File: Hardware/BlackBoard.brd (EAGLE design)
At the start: 68.6 x 53.3 mm, 72 parts, among them IC3 LM1117, J1 microB, J2 ICSP, J3 POWER_JACKSUPER_BOMB_DIGITY, Q1 1A/60V/500mΩ, Q2 2N7002PW, Q3 2N7002PW, U2 CH340G, U3 AP2112-3.3V, U4 ATMEGA328P_TQFP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

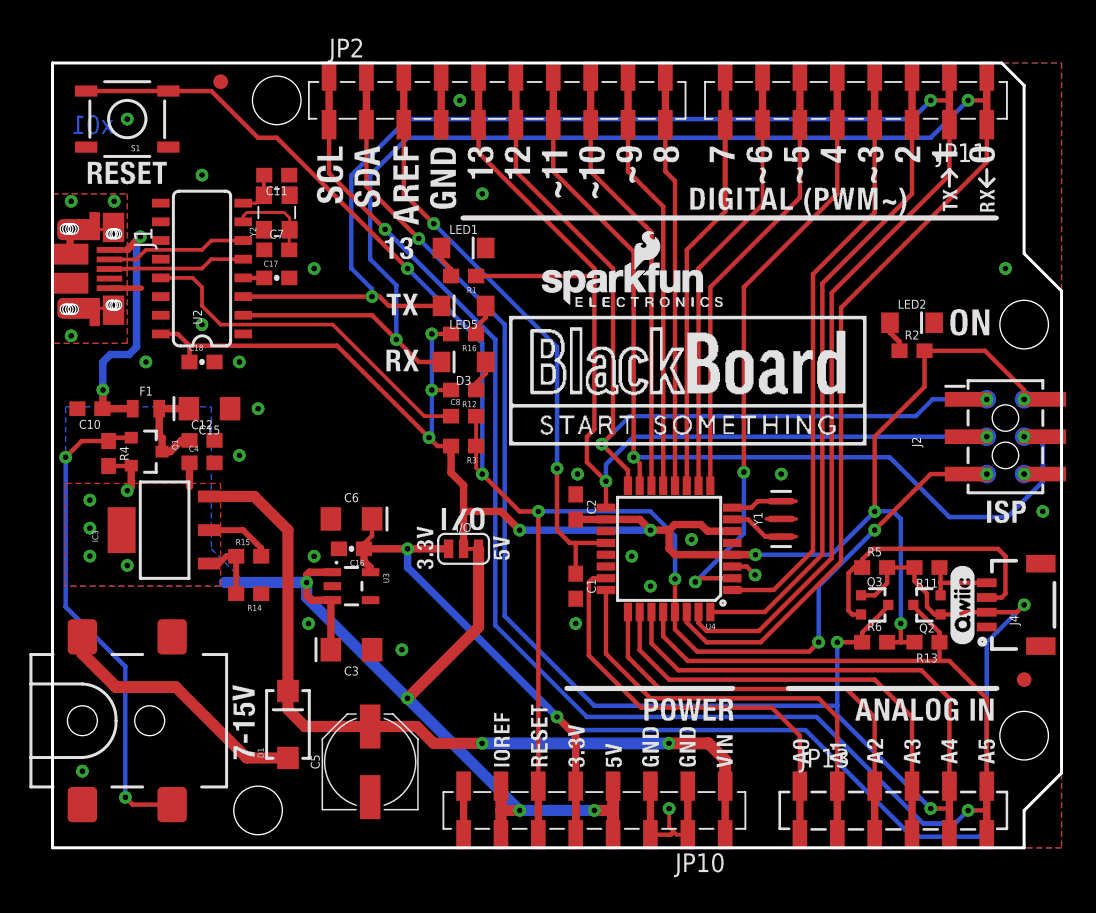
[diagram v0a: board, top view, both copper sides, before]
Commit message: Readme update. Schematic compression.
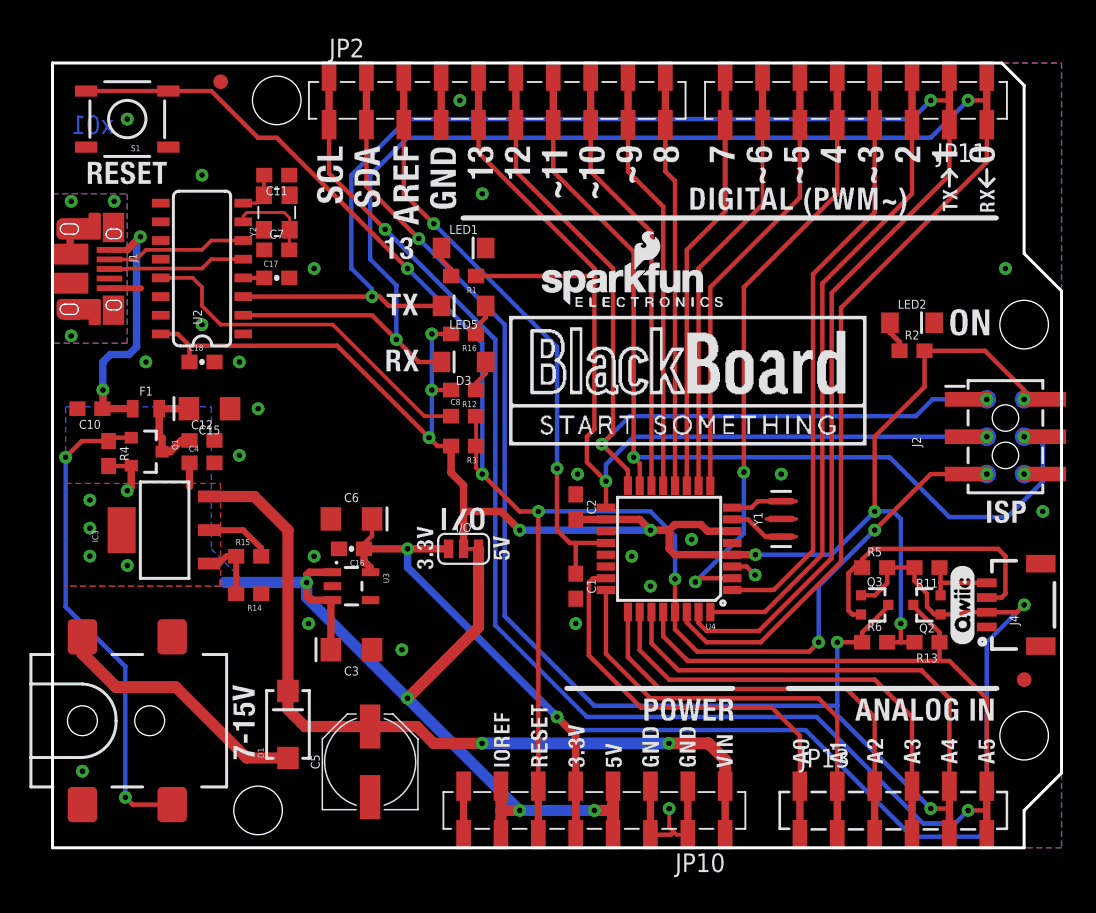
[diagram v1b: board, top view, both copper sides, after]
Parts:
- removed FRAME1: FRAME-LEDGER, SparkFun-Aesthetics:CREATIVE_COMMONS
- added FRAME2: FRAME-LETTER, SparkFun-Aesthetics:CREATIVE_COMMONS
- D1: value MBRA140 -> SS14TR
- J1: value microB -> AMP FCI 10103594-0001LF; device SparkFun-Connectors:USB-MICROB-PTH -> SparkFun-Connectors:USB-MICROB-PTH-MILL
- J2: value ICSP -> ISP
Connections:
- net SHLD: now also J1.SHIELD2, J1.SHIELD7; no longer J1.7, J1.SHEILD2, J1.SHIELD11, J1.SHIELD12
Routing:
- net SHLD: track 7.89 -> 1.48 mm
- net AD5/SCL: track 115.7 -> 120.6 mm
- net AD4/SDA: track 115.8 -> 120.6 mm
- net SCK: track 67.2 -> 70.8 mm
- net SS: track 26.2 -> 29.5 mm
- net MISO: track 57.0 -> 60.3 mm
- net IO9: track 25.5 -> 28.8 mm
- net IO8: track 24.8 -> 28.1 mm
- net IO6: track 26.3 -> 29.6 mm
- net IO4: track 37.7 -> 41.0 mm
- net IO2: track 41.0 -> 44.3 mm
- net AREF: track 37.7 -> 41.0 mm
- net AD3: track 27.7 -> 31.0 mm
- net AD1: track 26.5 -> 29.8 mm
- net TX-O: track 111.8 -> 115.1 mm
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
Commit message: Add USB pads for external connector
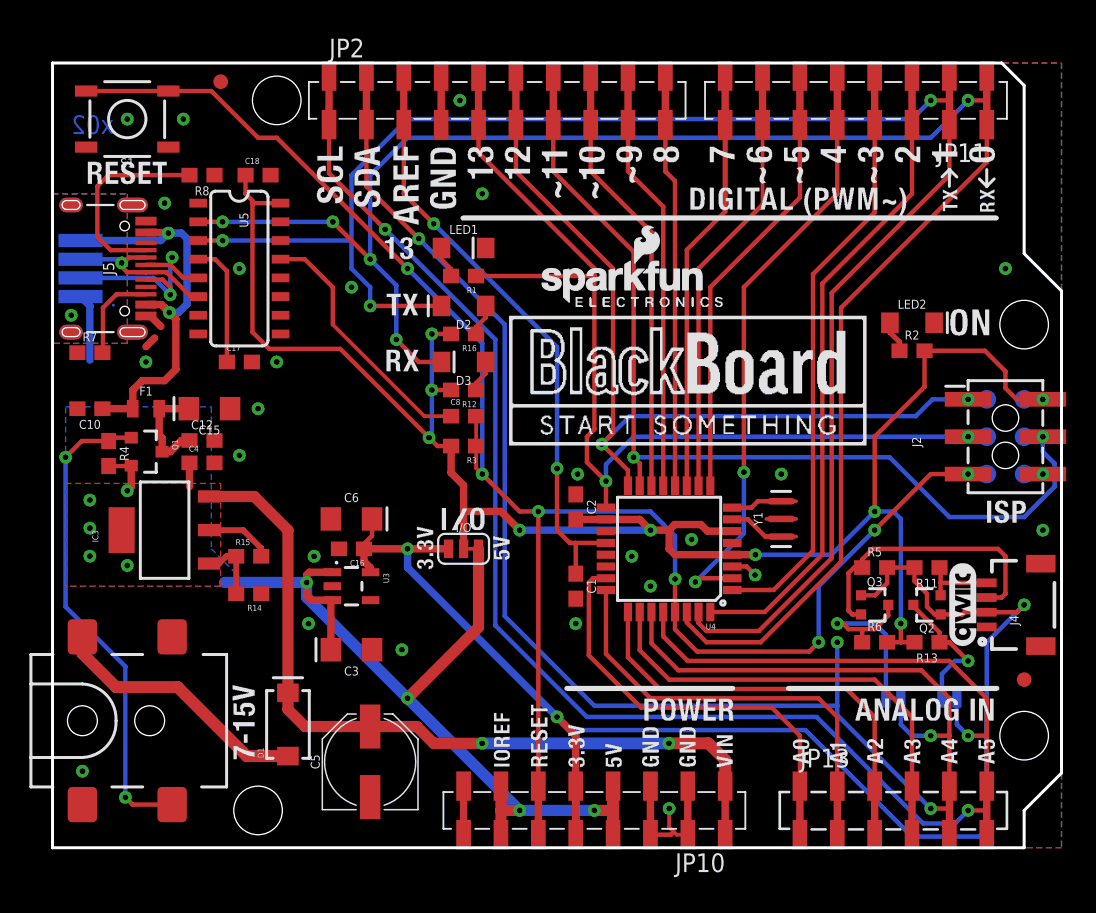
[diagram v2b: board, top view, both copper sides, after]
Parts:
- removed C11, C7: 22pF, SparkFun-Capacitors:0603
- removed FRAME2: FRAME-LETTER, SparkFun-Aesthetics:CREATIVE_COMMONS
- removed J1: AMP FCI 10103594-0001LF, SparkFun-Connectors:USB-MICROB-PTH-MILL
- removed LED5: GREEN, SparkFun-LED:LED-1206-HIDDENSILK
- removed U2: CH340G, SparkFun-DigitalIC:SO016
- removed Y2: 12MHz, USB Basic:CRYSTAL-SMD-3.2X2.5
- added D2: GREEN, SparkFun-LED:LED-1206
- added FRAME1: FRAME-LETTER, SparkFun-Aesthetics:CREATIVE_COMMONS
- added J5: USB C, USB-C:USB-C-16P
- added JP14: USB_SOLDER_PADS, SparkFun-Connectors:USB-SOLDER-PADS
- added QW1, QW2: (no value), SparkFun-Jumpers:SMT-JUMPER_2_NC_TRACE_SILK
- added R7, R8: 5.1k, SparkFun-Resistors:0603
- added U$10: (no value), buzzard_labels (14):D#4
- added U$11: (no value), buzzard_labels (13):G1
- added U$12: (no value), buzzard_labels (13):V0
- added U$9: (no value), Labels:QWIIC_COPYRIGHT_SMALL
- added U5: CH340C, SparkFun-IC-Comms:SO016
- C16, C17, C18: device SparkFun-Capacitors:0603-CAP -> SparkFun-Capacitors:0603
- D1: value SS14TR -> 1A/40V/500mV
- F1: value PPTC_6V500MA -> 6V 0.5A
- LED2: device SparkFun-LED:LED-1206-HIDDENSILK -> SparkFun-LED:LED-1206
- Q1: value 1A/60V/500mΩ -> 1.1A/60V/600mΩ
- Q2, Q3: value 2N7002PW -> 310mA/60V/1.6Ω
- S1: value RESET -> Tall Switch; device SparkFun-Electromechanical:TACTILE-SWITCH-SMD -> SparkFun-Switches:TACTILE_SWITCH_SMD_5.2MM
- U$2: device Labels-0_04:(QWIIC) -> buzzard_labels (14):D#3
- moved U$2 61.6 mm to (5.59, 38.7), flipped to the bottom, turned to 0 degrees
- moved C18 13.3 mm to (14.0, 45.7)
- moved JP1 6.28 mm to (38.7, 38.5)
- moved C17 6.25 mm to (12.7, 33.0)
- moved JP7 2.32 mm to (40.4, 41.0)
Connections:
- removed net N$11: C11.2, U2.8, Y2.3
- removed net N$12: C7.2, U2.7, Y2.1
- removed net N$13: J1.D-, U2.6
- removed net N$14: J1.D+, U2.5
- removed net V3: C17.1, U2.4
- new net CC1: J5.A5, R8.2
- new net CC2: J5.B5, R7.2
- new net D+: J5.A6, J5.B6, JP14.D+, U5.5
- new net D-: J5.A7, J5.B7, JP14.D-, U5.6
- new net N$45: Q3.3, QW2.2, R6.1
- new net N$6: C17.1, U5.4
- new net N$7: Q2.3, QW1.2, R13.1
- net !DTR: now also U5.13; no longer U2.13
- net AD4/SDA: now also QW2.1; no longer Q3.3, R6.1
- net AD5/SCL: now also QW1.1; no longer Q2.3, R13.1
- net GND: now also J5.GND, J5.GND2, JP14.GND, R7.1, R8.1, U5.1; no longer C11.1, C7.1, J1.GND, U2.1, Y2.2, Y2.4
- net N$5: now also D2.A; no longer LED5.A
- net RX-I: now also U5.2; no longer U2.2
- net SHLD: now also J5.SHLD1, J5.SHLD2, J5.SHLD3, J5.SHLD4, J5.SHLD5, J5.SHLD6, J5.SHLD7, J5.SHLD8; no longer J1.SHIELD, J1.SHIELD10, J1.SHIELD2, J1.SHIELD3, J1.SHIELD4, J1.SHIELD5, J1.SHIELD6, J1.SHIELD7, J1.SHIELD8, J1.SHIELD9
- net TX-O: now also D2.C, U5.3; no longer LED5.C, U2.3
- net VCC: now also U5.16; no longer U2.16
- net VUSB: now also J5.VBUS1, J5.VBUS2, JP14.VBUS; no longer J1.VBUS
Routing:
- net D+: track 0.00 -> 16.0 mm, vias 0 -> 2
- net CC1: track 0.00 -> 13.7 mm
- net N$45: track 0.00 -> 13.6 mm, vias 0 -> 1
- net D-: track 0.00 -> 11.0 mm, vias 0 -> 1
- net VUSB: track 18.0 -> 27.7 mm
- net N$13: track 9.62 -> 0.00 mm
- net N$7: track 0.00 -> 9.54 mm, vias 0 -> 1
- net N$14: track 9.37 -> 0.00 mm
- net N$6: track 0.00 -> 8.47 mm
- net VCC: track 116.5 -> 123.6 mm
- net !DTR: track 24.4 -> 17.5 mm
- net CC2: track 0.00 -> 6.36 mm
- net N$12: track 5.99 -> 0.00 mm
- net GND: track 8.37 -> 12.9 mm, vias 25 -> 26
- net N$11: track 3.00 -> 0.00 mm
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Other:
- board text added: "x02"
- board text removed: "Based on Arduino by: M. Banzi, D. Cuartielles, T. Igoe, G. Martino, D. Mellis"
- board text removed: "J. Lindblom, N. Seidle"
- board text removed: "x01"
